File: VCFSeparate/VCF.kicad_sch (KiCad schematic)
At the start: 29 parts, among them U1 LM13700, U2 LM13700

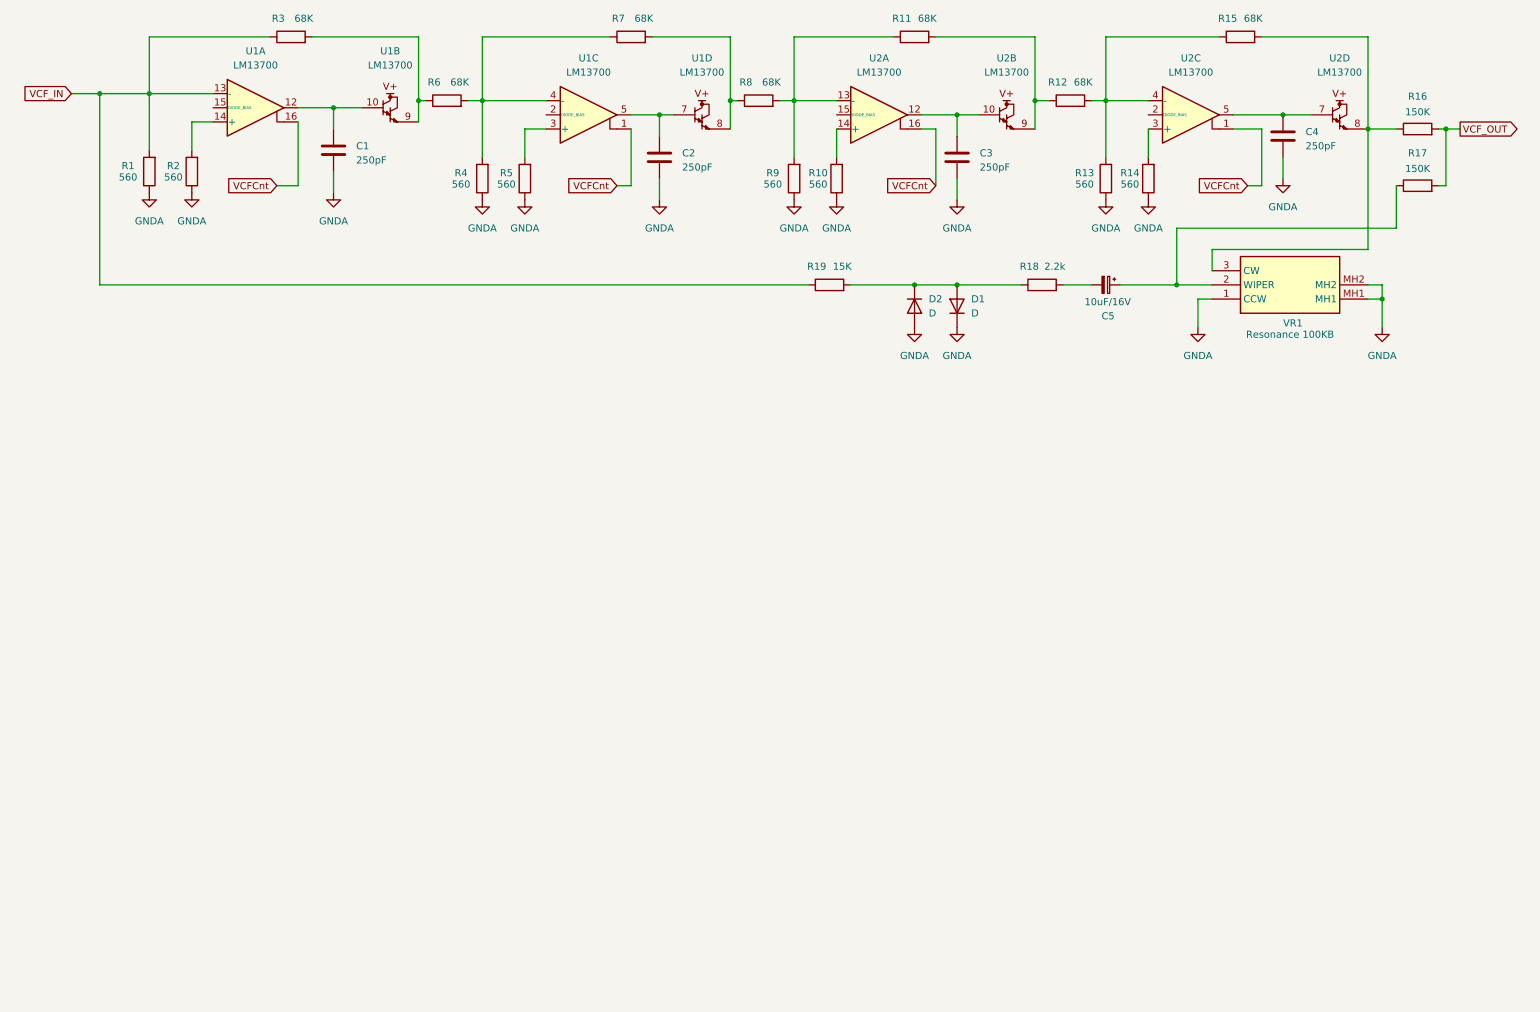
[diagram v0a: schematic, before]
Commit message: VCFSeparate
レゾナンスVCAを追加
コントローラー系を作成中
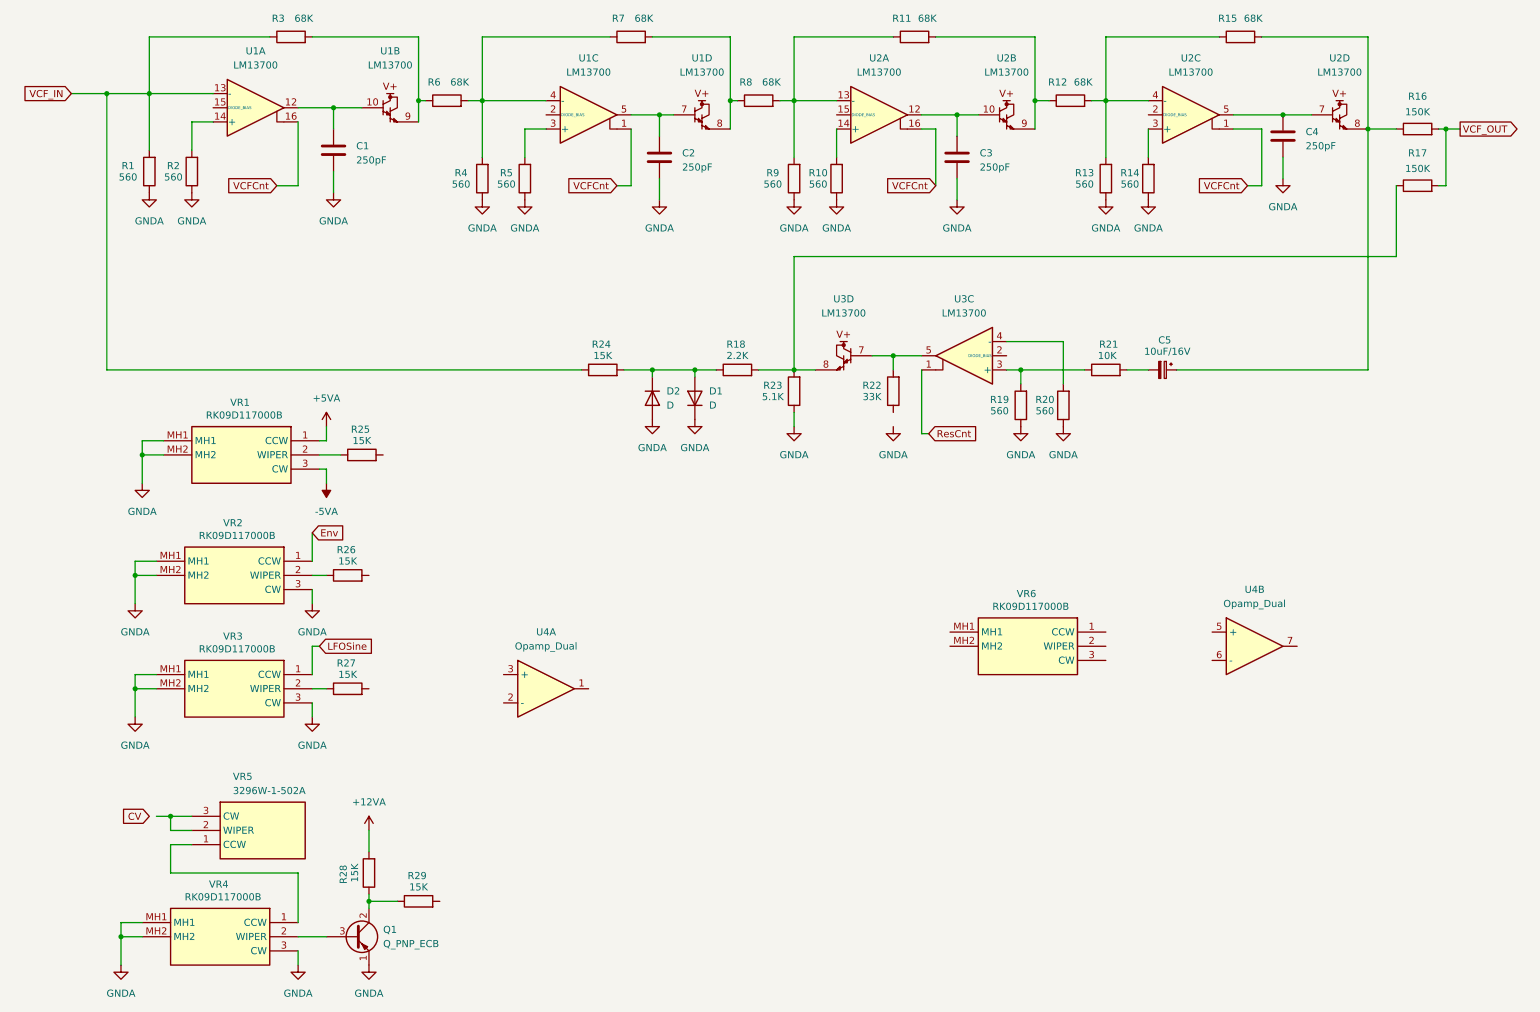
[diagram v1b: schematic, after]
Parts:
- added Q1: Q_PNP_ECB, symbol Device:Q_PNP_ECB
- added R20: 560, Resistor_THT:R_Axial_DIN0204_L3.6mm_D1.6mm_P2.54mm_Vertical, symbol Device:R
- added R21: 10K, Resistor_THT:R_Axial_DIN0204_L3.6mm_D1.6mm_P2.54mm_Vertical, symbol Device:R
- added R22: 33K, Resistor_THT:R_Axial_DIN0204_L3.6mm_D1.6mm_P2.54mm_Vertical, symbol Device:R
- added R23: 5.1K, Resistor_THT:R_Axial_DIN0204_L3.6mm_D1.6mm_P2.54mm_Vertical, symbol Device:R
- added R24, R25, R26, R27, R28, R29: 15K, Resistor_THT:R_Axial_DIN0204_L3.6mm_D1.6mm_P2.54mm_Vertical, symbol Device:R
- added U3: LM13700, Package_SO:SOIC-16_3.9x9.9mm_P1.27mm, symbol Amplifier_Operational:LM13700
- added U4: Opamp_Dual, Package_DIP:DIP-8_W7.62mm_LongPads, symbol Device:Opamp_Dual
- added VR2, VR3, VR4, VR6: RK09D117000B, RK09D117000B, symbol SamacSys_Parts:RK09D117000B
- added VR5: 3296W-1-502A, 3296W1502A, symbol SamacSys_Parts:3296W-1-502A
- R18: value 2.2k -> 2.2K
- R19: value 15K -> 560
- VR1: value Resonance 100KB -> RK09D117000B
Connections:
- net GNDA: now also R19.1, Q1.1 (E), R20.1, R23.1, VR2.3 (CW), VR2.MH1, VR2.MH2, VR3.3 (CW), VR3.MH1, VR3.MH2, VR4.3 (CW), VR4.MH1, VR4.MH2; no longer VR1.1 (CCW)
- net VCF_IN: now also R24.1; no longer R19.1
- net at R15.2, R16.1, U2.8: now also C5.1; no longer VR1.3 (CW)
- net at D1.2 (A), D2.1 (K), R18.1: now also R24.2; no longer R19.2
- net at R18.2: now also R17.1, R23.2, U3.8; no longer C5.2
- new net: R20.2, U3.4 (-)
- new net: R26.1, VR2.2 (WIPER)
- new net: R19.2, R21.1, U3.3 (+)
- new net: R22.2, U3.5, U3.7
- new net: R27.1, VR3.2 (WIPER)
- new net: VR4.1 (CCW), VR5.1 (CCW)
- new net: VR5.2 (WIPER), VR5.3 (CW)
- new net: Q1.3 (B), VR4.2 (WIPER)
- new net: Q1.2 (C), R28.1, R29.1
- new net: C5.2, R21.2
- new net: R25.1, VR1.2 (WIPER)
- new net +12VA: R28.2
- new net +5VA: VR1.1 (CCW)
- new net -5VA: VR1.3 (CW)
- new net Env: VR2.1 (CCW)
- new net LFOSine: VR3.1 (CCW)
- new net ResCnt: U3.1
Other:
- moved on the sheet: C5, D1, D2

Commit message: MC2
VCO,VCF+VCA,Powerを登録
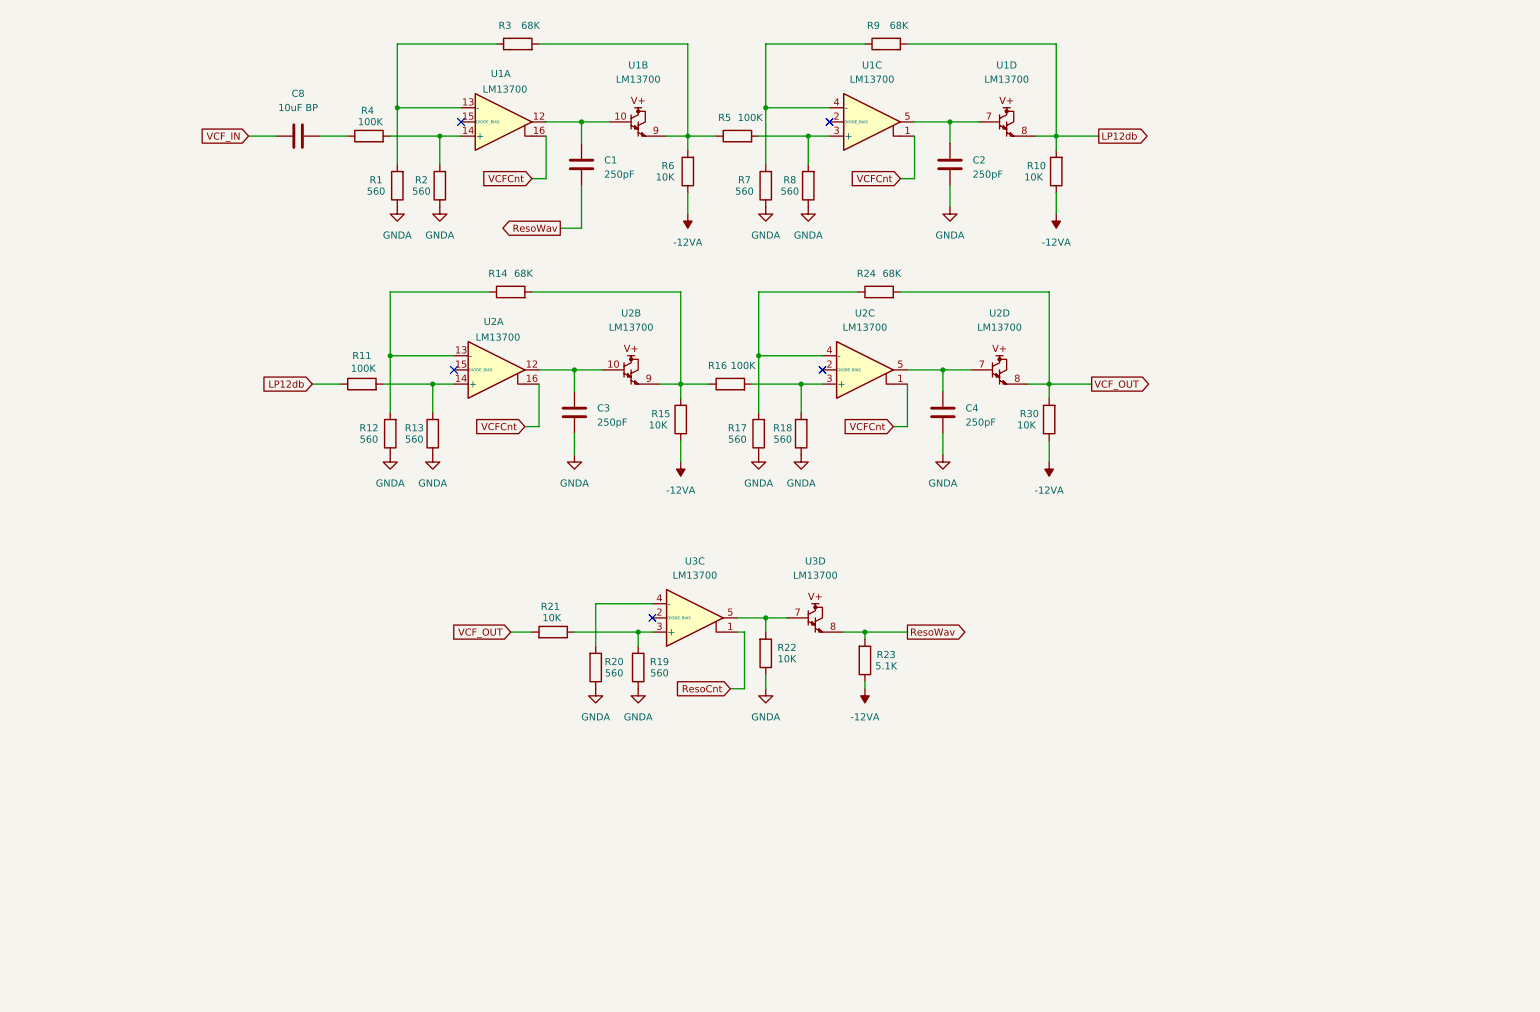
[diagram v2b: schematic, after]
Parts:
- removed C5: 10uF/16V, Capacitor_THT:CP_Radial_D5.0mm_P2.50mm, symbol Device:C_Polarized_Small
- removed D1, D2: D, Diode_THT:D_DO-34_SOD68_P2.54mm_Vertical_AnodeUp, symbol Device:D
- removed Q1: Q_PNP_ECB, symbol Device:Q_PNP_ECB
- removed R25, R26, R27, R28, R29: 15K, Resistor_THT:R_Axial_DIN0204_L3.6mm_D1.6mm_P2.54mm_Vertical, symbol Device:R
- removed U4: Opamp_Dual, Package_DIP:DIP-8_W7.62mm_LongPads, symbol Device:Opamp_Dual
- removed VR1, VR2, VR3, VR4, VR6: RK09D117000B, RK09D117000B, symbol SamacSys_Parts:RK09D117000B
- removed VR5: 3296W-1-502A, 3296W1502A, symbol SamacSys_Parts:3296W-1-502A
- added C8: 10uF BP, Capacitor_THT:C_Radial_D5.0mm_H5.0mm_P2.00mm, symbol Device:C
- added R30: 10K, Resistor_THT:R_Axial_DIN0204_L3.6mm_D1.6mm_P2.54mm_Vertical, symbol Device:R
- R10: value 560 -> 10K
- R11: value 68K -> 100K
- R12, R7, R8: value 68K -> 560
- R14, R9: value 560 -> 68K
- R15, R6: value 68K -> 10K
- R16: value 150K -> 100K
- R17: value 150K -> 560
- R18: value 2.2K -> 560
- R22: value 33K -> 10K
- R24: value 15K -> 68K
- R4, R5: value 560 -> 100K
- U1: footprint Package_SO:SOIC-16_3.9x9.9mm_P1.27mm -> (none)
- U2: footprint (none) -> Package_SO:SOIC-16_3.9x9.9mm_P1.27mm
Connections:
- net GNDA: now also R12.1, R17.1, R18.1, R22.1, R7.1, R8.1; no longer C1.2, R10.1, R14.1, R23.1, R4.1, R5.1, R9.1
- net VCF_IN: now also C8.1; no longer R1.2, R24.1, R3.1, U1.13 (-)
- net VCF_OUT: now also R21.2, R24.2, U2.8, R30.2; no longer R16.2, R17.2
- net at R15.2, R16.1: now also R14.2, U2.9; no longer U2.8
- net at R3.2, U1.9: now also R5.1, R6.2; no longer R6.1
- net LP12db: now reaches R11.1, R9.2
- net LP12db: now also R10.2, U1.8; no longer R8.2, U2.13 (-)
- net at R5.2, U1.3 (+): now also R8.2
- net ResoWav: now reaches R23.2, U3.8
- net ResoWav: now also C1.2; no longer R17.1, R18.2
- net at R2.2, U1.14 (+): now also R4.2
- net at U2.14 (+): now also R11.2, R13.2; no longer R10.2
- net at U2.3 (+): now also R16.2, R18.2; no longer R14.2
- net ResCnt renamed ResoCnt
- new net: R17.2, R24.1, U2.4 (-)
- new net: R7.2, R9.1, U1.4 (-)
- new net: C8.2, R4.1
- new net: R1.2, R3.1, U1.13 (-)
- new net: R12.2, R14.1, U2.13 (-)
- new net -12VA: R10.1, R15.1, R23.1, R30.1, R6.1
- no-connect marks 0 -> 5
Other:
- moved on the sheet: C1, R1, R19, R2, R20, R21, R22, R23, R3, R6, U1A, U1B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
